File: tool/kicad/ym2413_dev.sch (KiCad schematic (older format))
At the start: 61 parts, among them P1 CONN_4, U1 YM2413, X1 CRYSTAL

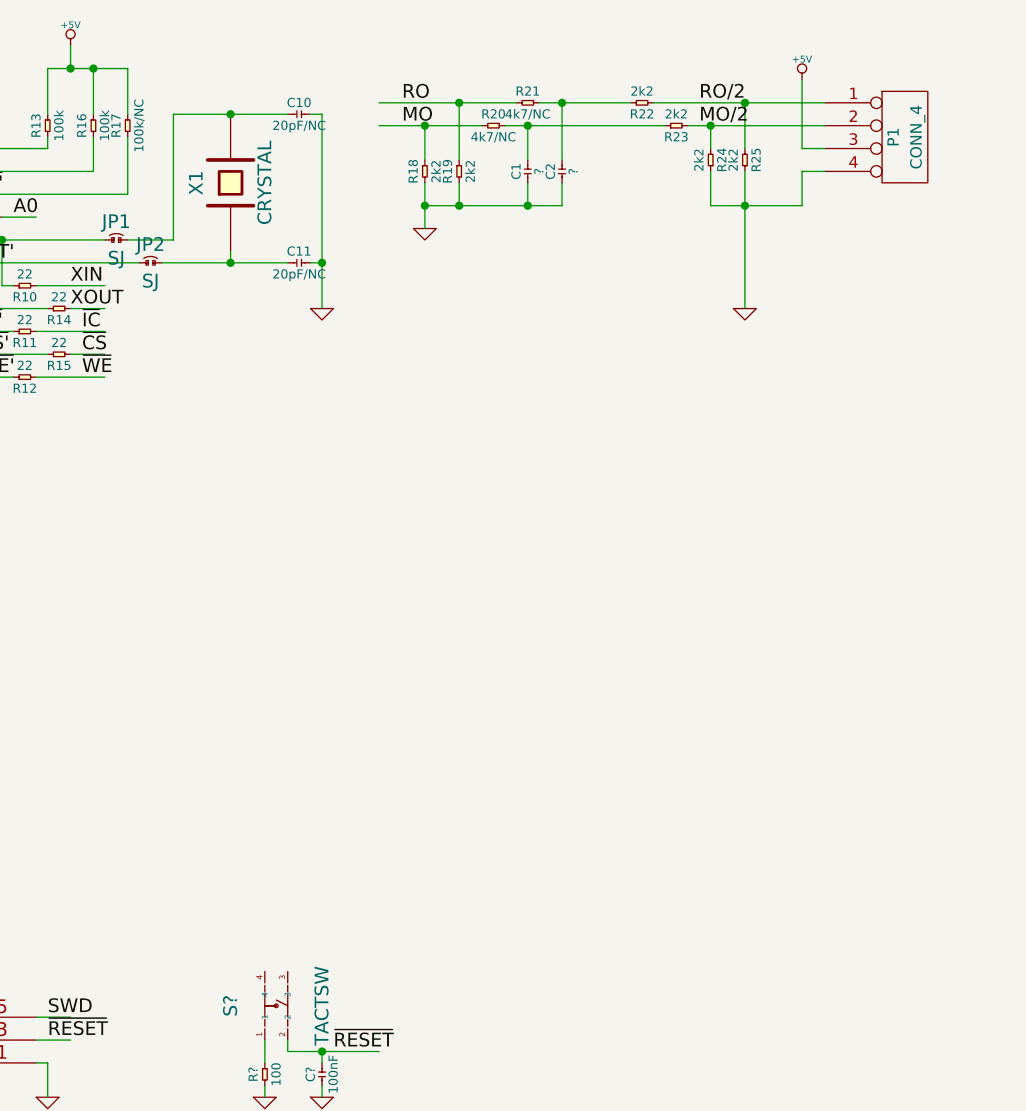
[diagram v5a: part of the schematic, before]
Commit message: add optional audio amplifier output circuitry
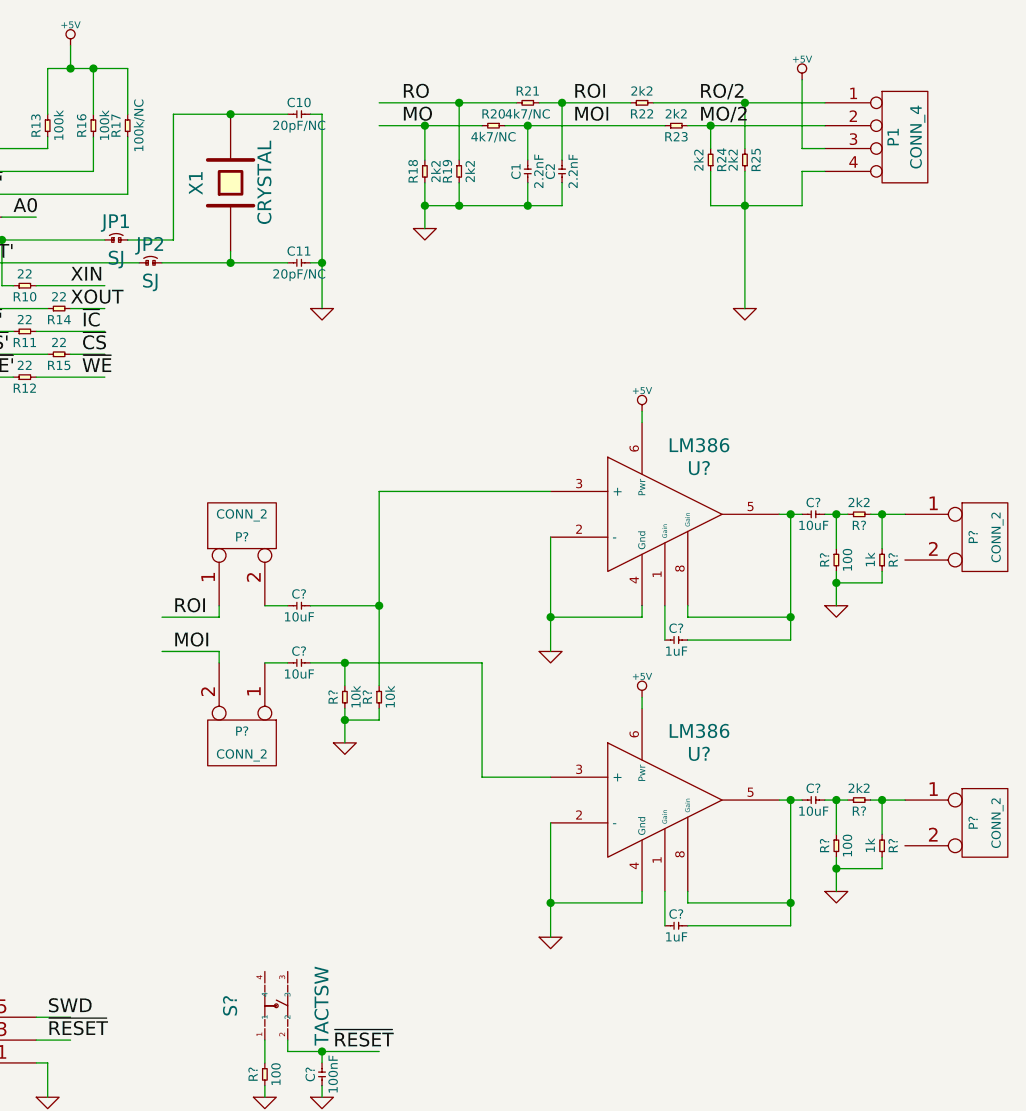
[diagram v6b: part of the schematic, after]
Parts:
- added C? (x4): 10uF, symbol C
- added C? (x2): 1uF, symbol C
- added P? (x4): CONN_2, symbol CONN_2
- added R? (x2): 10k, symbol R
- added R? (x2): 100, symbol R
- added R? (x2): 2k2, symbol R
- added R? (x2): 1k, symbol R
- added U? (x2): LM386, symbol LM386
- C1, C2: value ? -> 2.2nF
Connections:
- net labels added: MOI, ROI
- wire segments 179 -> 229

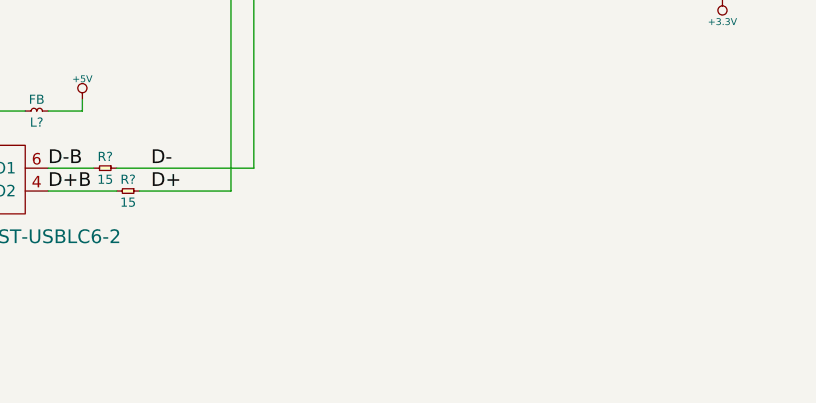
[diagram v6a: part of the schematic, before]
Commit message: add optocoupled midi in
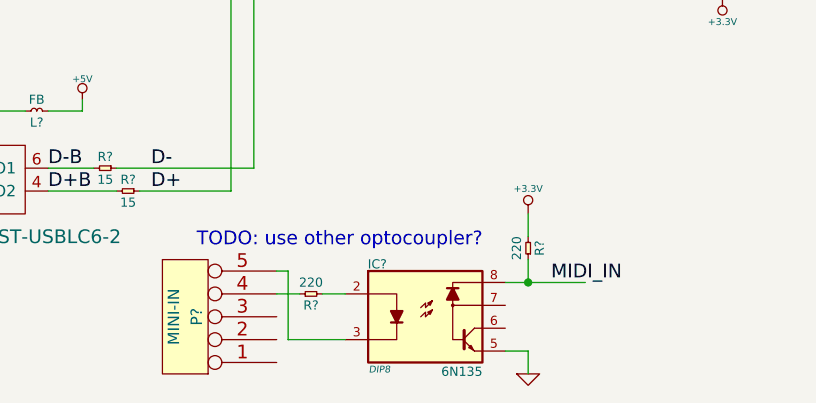
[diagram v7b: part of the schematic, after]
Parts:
- added IC?: 6N135, DIP8, symbol 6N135
- added P?: MINI-IN, symbol CONN_5
- added R? (x2): 220, symbol R
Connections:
- net labels added: MIDI_IN
- wire segments 229 -> 239
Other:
- note added: "TODO: use other optocoupler?"

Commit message: add midi protection diode
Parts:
- added D?: D, symbol D
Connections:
- wire segments 239 -> 241
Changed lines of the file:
@@
 Text Notes 3800 7000 0    60   ~ 0
 TODO: use other optocoupler?
+$Comp
+L D D?
+U 1 1 52F758D1
+P 4400 7300
+F 0 "D?" V 4350 7400 60  0000 C CNN
+F 1 "D" H 4405 7235 60  0001 C CNN
+F 2 "" H 4400 7300 60  0000 C CNN
+F 3 "" H 4400 7300 60  0000 C CNN
+	1    4400 7300
+	0    -1   -1   0
+$EndComp
+Wire Wire Line
+	4400 7200 4400 7250
+Connection ~ 4400 7200
+Wire Wire Line
+	4400 7350 4400 7400
+Connection ~ 4400 7400
 $EndSCHEMATC
